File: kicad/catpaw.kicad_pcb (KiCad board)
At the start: 2 copper layers, 80 x 75 mm, 34 parts, among them J3 m12,Acode,5pin,femalesocket (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, J4 m8, 4Pin Supply Connector FEM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, SW1 1MD1T1B1M6QES, U1 INA826, U2 LM1458mx

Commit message: pcbnew initial route
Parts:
- C1, R1, R2, R3, R8, U1: moved to B.Cu
- C2: renamed from C3; moved to B.Cu
- R10: renamed from R9; moved to B.Cu
- R11: renamed from R10; moved to B.Cu
- R4: renamed from R5; moved to B.Cu
- R5: renamed from R6; moved to B.Cu
- R6: renamed from R7; moved to B.Cu
- R7: renamed from R4; moved to B.Cu
- R9: renamed from R11; moved to B.Cu
- moved R14 86.1 mm to (126.0, 45.5)
- moved R12 84.8 mm to (142.3, 49.5), turned to -90 degrees
- moved R13 82.7 mm to (145.3, 49.5), turned to -90 degrees
- moved R15 78.6 mm to (126.0, 48.0), turned to 180 degrees
- moved R16 78.0 mm to (126.0, 51.6), turned to 180 degrees
- moved C3 77.0 mm to (132.0, 45.2)
- moved U2 75.7 mm to (132.3, 49.0)
- moved C4 72.4 mm to (129.8, 53.7), turned to 90 degrees
- moved R1 67.2 mm to (139.6, 84.6)
- moved R2 67.2 mm to (145.2, 84.6)
- moved R3 67.2 mm to (150.8, 84.6)
- moved C2 66.0 mm to (170.3, 84.8)
- moved R8 64.1 mm to (156.2, 85.9)
- moved R11 59.7 mm to (172.4, 88.1), turned to 90 degrees
- moved R7 59.4 mm to (152.6, 88.9), turned to -90 degrees
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- renumbered C2 to C3, red to J1, blk to J2
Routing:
- net /Vcc+: track 0.00 -> 98.0 mm, vias 0 -> 3
- net /Vcc-: track 0.00 -> 87.1 mm, vias 0 -> 1
- net /rakout+: track 0.00 -> 43.8 mm
- net /rakout-: track 0.00 -> 41.1 mm
- net Net-(D5-A): track 0.00 -> 20.9 mm, vias 0 -> 1
- net Net-(PS1-AC(L)): track 17.2 -> 0.00 mm
- net /In+ Analog Input: track 0.00 -> 16.9 mm
- net Net-(F1-Pad1): track 18.3 -> 3.17 mm
- net Net-(PS1-AC(N)): track 14.2 -> 0.00 mm
- net Net-(D5-K): track 0.00 -> 13.5 mm, vias 0 -> 1
- net Net-(U2B-+): track 0.00 -> 11.5 mm
- net Net-(U2A-+): track 0.00 -> 8.37 mm
- net GND: track 0.00 -> 7.24 mm
- added copper zone on B.Cu, net GND
- added copper zone on F.Cu, net GND

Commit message: pcbnew route v02
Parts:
- C3, C4, R12, R13, R14, R15, R16, U2: moved to B.Cu
- moved R15 34.3 mm to (148.8, 73.5), turned to 0 degrees
- moved R16 33.8 mm to (148.2, 77.1), turned to 0 degrees
- moved C4 28.7 mm to (143.6, 78.9), turned to 0 degrees
- moved U2 27.3 mm to (141.9, 74.5), turned to 180 degrees
- moved C3 25.7 mm to (139.4, 69.8), turned to -90 degrees
- moved R12 12.4 mm to (137.4, 61.0), turned to 90 degrees
- moved R13 11.7 mm to (147.6, 61.0), turned to 90 degrees
- moved C1 2.54 mm to (168.5, 94.7)
- moved R14 2.40 mm to (124.0, 46.7)
- moved R11 2.21 mm to (173.2, 90.2)
- moved R10 2.03 mm to (160.3, 90.6)
- moved R8 2.03 mm to (156.2, 87.9)
- moved R9 2.03 mm to (156.2, 93.2)
- moved U1 2.03 mm to (166.6, 90.6)
- moved C2 1.88 mm to (169.7, 86.6)
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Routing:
- net /Vcc+: track 98.0 -> 60.9 mm
- net /Vcc-: track 87.1 -> 50.2 mm, vias 1 -> 2
- net Net-(PS1-AC(L)): track 0.00 -> 27.4 mm
- net Net-(D5-A): track 20.9 -> 43.5 mm
- net /VACin+: track 22.9 -> 44.7 mm
- net Net-(U2B-+): track 11.5 -> 28.2 mm
- net /VACin-: track 42.6 -> 55.6 mm
- net /m8 GNDp: track 0.00 -> 12.8 mm
- net /m8 Up: track 0.00 -> 11.8 mm
- net Net-(PS1-AC(N)): track 0.00 -> 9.51 mm
- net /m8 GNDs: track 0.00 -> 9.06 mm
- net /m8 Us: track 0.00 -> 9.00 mm
- net Net-(U1--): track 0.00 -> 7.24 mm
- net Net-(U1-+): track 0.00 -> 7.24 mm
- net GND: track 7.24 -> 0.00 mm, vias 0 -> 138
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- added copper zone on B.Cu, net /Vcc+
- added copper zone on B.Cu, net /Vcc-
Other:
- board text added: "blk"
- board text added: "red"

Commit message: pcbnew route03
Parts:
- moved C3 3.94 mm to (143.4, 69.8)
- moved C4 3.94 mm to (147.5, 78.9)
- moved R15 3.94 mm to (152.8, 73.5)
- moved R16 3.94 mm to (152.2, 77.1)
- moved U2 3.94 mm to (145.8, 74.5)
- moved R1 1.02 mm to (139.6, 87.4)
- moved R2 1.02 mm to (145.2, 87.4)
- moved R3 1.02 mm to (150.8, 87.4)
- moved R4 1.02 mm to (139.7, 96.0)
- moved R5 1.02 mm to (145.3, 96.0)
- moved R6 1.02 mm to (150.8, 96.0)
- moved R7 1.02 mm to (152.4, 91.7)
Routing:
- net Net-(D5-A): track 43.5 -> 51.9 mm
- net /Vcc+: track 60.9 -> 56.9 mm
- net /Vcc-: track 50.2 -> 46.3 mm
- net /VACin+: track 44.7 -> 47.4 mm
- net /VACin-: track 55.6 -> 56.8 mm
- net GND: vias 138 -> 121
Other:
- board text added: "M12"
- board text added: "M8"
- board text added: "catpaw rev01 jul26 //keyudits"

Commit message: Exported BOM01, notes to scheme, touched up pcbnew
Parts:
- removed D3, D4: 1N5819, Diode_THT:D_DO-41_SOD81_P10.16mm_Horizontal
- D5: footprint Diode_THT:D_5W_P5.08mm_Vertical_AnodeUp -> LED_THT:LED_D5.0mm_Horizontal_O1.27mm_Z3.0mm
- moved R14 7.39 mm to (116.6, 47.5)
- moved D5 2.75 mm to (111.8, 47.5), turned to -90 degrees
- moved D1 0.25 mm to (172.7, 58.4)
- moved D2 0.25 mm to (169.0, 58.4)
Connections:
- J4 pad 3: /m8 GNDs -> /m8 GNDp
- PS1 pad 4: /rakout- -> /m8 GNDp
- R13 pad 2: /rakout- -> /m8 GNDp
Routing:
- net /rakout-: track 44.3 -> 0.00 mm
- net /m8 GNDp: track 12.8 -> 39.0 mm
- net /m8 GNDs: track 9.06 -> 0.00 mm
- net Net-(D5-K): track 10.9 -> 4.10 mm
- net Net-(D5-A): track 51.9 -> 58.7 mm
- net /Vcc+: track 56.9 -> 59.2 mm, vias 3 -> 8
- net /In+ Analog Input: track 15.4 -> 14.5 mm
- net /Vcc-: track 46.3 -> 47.2 mm, vias 2 -> 5
- net GND: vias 121 -> 127

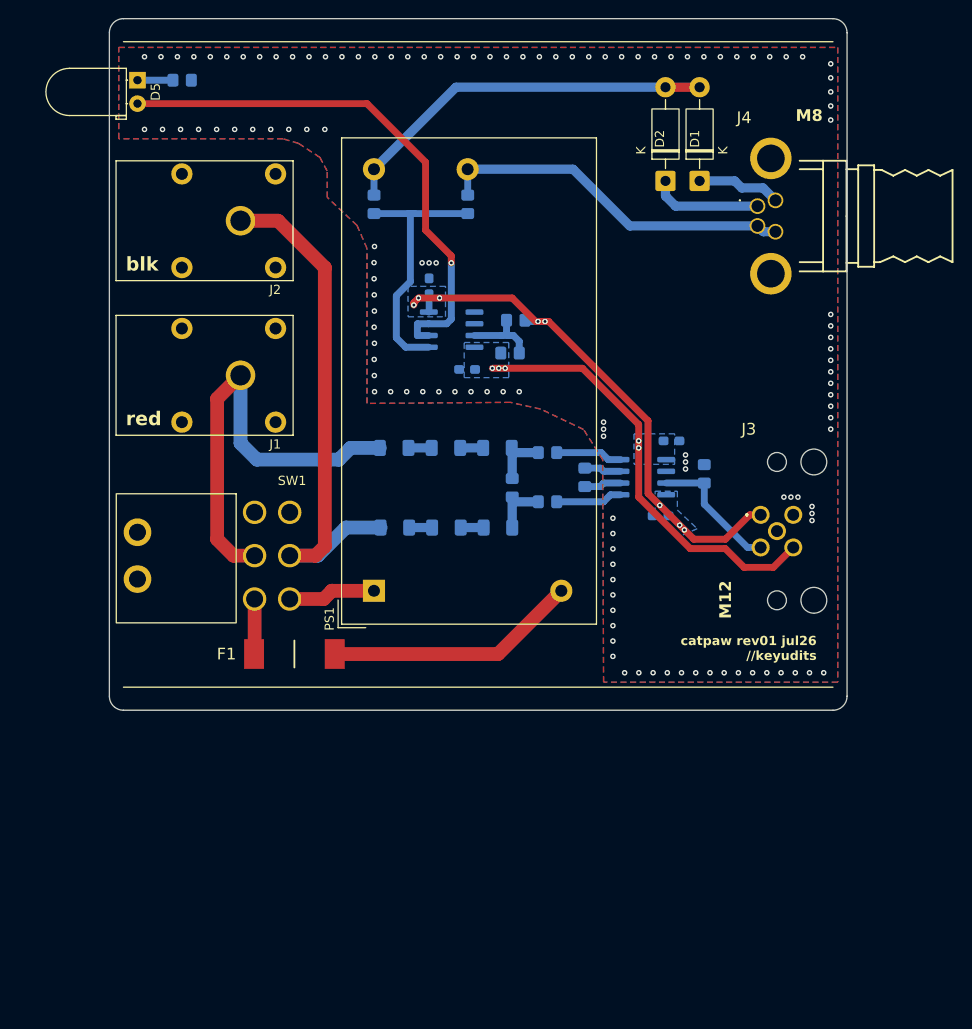
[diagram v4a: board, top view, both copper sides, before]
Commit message: adjusted i/o placement
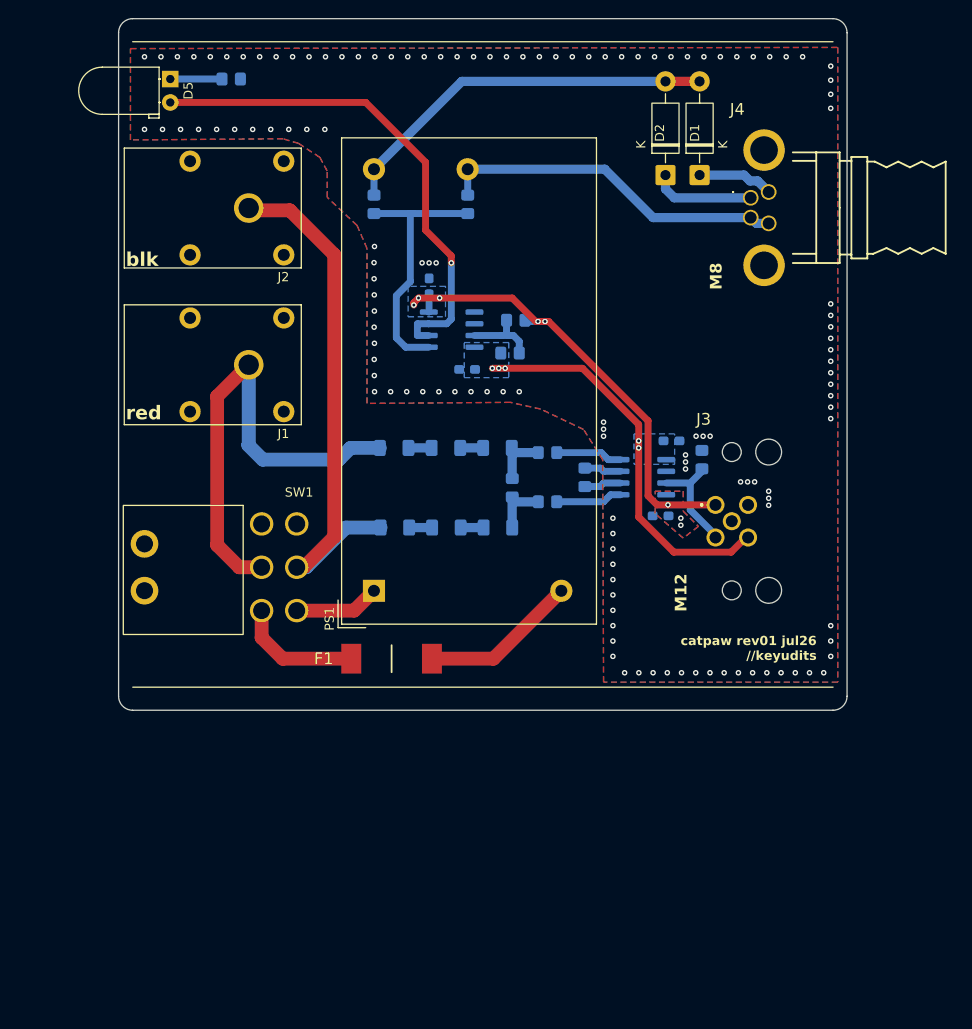
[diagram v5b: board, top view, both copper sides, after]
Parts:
- moved F1 10.6 mm to (139.3, 110.2)
- moved R14 5.32 mm to (121.9, 47.4)
- moved J3 5.02 mm to (174.4, 93.6)
- moved D5 3.56 mm to (115.3, 47.4)
- moved J2 1.64 mm to (123.8, 61.4)
- moved R11 1.56 mm to (173.0, 88.6)
- moved SW1 1.47 mm to (125.2, 100.4)
- moved J1 1.45 mm to (123.8, 78.4)
- moved J4 1.17 mm to (180.2, 59.6)
- moved D1 0.64 mm to (172.7, 57.8)
- moved D2 0.64 mm to (169.0, 57.8)
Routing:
- net Net-(PS1-AC(L)): track 27.4 -> 17.1 mm
- net Net-(F1-Pad1): track 6.03 -> 13.6 mm
- net /Vcc+: track 59.2 -> 51.8 mm
- net /Vcc-: track 47.2 -> 42.7 mm
- net Net-(D5-A): track 58.7 -> 54.9 mm
- net /VACin+: track 47.4 -> 51.0 mm
- net /In+ Analog Input: track 14.5 -> 11.5 mm
- net Net-(D5-K): track 4.10 -> 5.60 mm
- net /VACin-: track 56.8 -> 58.2 mm
- net /m8 GNDp: track 39.0 -> 37.9 mm
- net /m8 Us: track 9.11 -> 8.25 mm
- net /m8 Up: track 11.8 -> 11.1 mm
- net GND: vias 127 -> 132
- added copper zone on F.Cu, net /Vcc+
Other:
- board size 80 x 75 mm -> 79 x 75 mm
- board text added: "dimensions: 75mm wide (hammond callout) 79mm long (1mm less than hammond case)"

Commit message: added test points and jumpers
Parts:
- added GND: Conn_01x01_Pin, Connector_PinHeader_2.54mm:PinHeader_1x01_P2.54mm_Vertical, F.Cu at (182.4, 76.8)
- added R18: 0, Resistor_THT:R_Axial_DIN0204_L3.6mm_D1.6mm_P2.54mm_Vertical, F.Cu at (171.1, 75.6)
- added R19: 0, Resistor_THT:R_Axial_DIN0204_L3.6mm_D1.6mm_P2.54mm_Vertical, F.Cu at (175.3, 75.6)
- added VCC: 0, Resistor_SMD:R_0805_2012Metric_Pad1.20x1.40mm_HandSolder, F.Cu at (168.1, 76.6)
- added VEE: 0, Resistor_SMD:R_0805_2012Metric_Pad1.20x1.40mm_HandSolder, F.Cu at (178.2, 76.6)
- moved R1 0.66 mm to (138.9, 87.4)
- moved R4 0.66 mm to (139.0, 96.0)
- moved R2 0.34 mm to (144.9, 87.4)
- moved R5 0.33 mm to (144.9, 96.0)
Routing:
- net /m8 Up: track 11.1 -> 32.7 mm
- net /m8 GNDp: track 37.9 -> 55.2 mm
- net /Vcc-: track 42.7 -> 55.9 mm, vias 5 -> 6
- net /Vcc+: track 51.8 -> 60.6 mm
- net /VACin-: track 58.2 -> 57.5 mm
- net /VACin+: track 51.0 -> 50.3 mm
- net GND: vias 132 -> 135
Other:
- board text added: "JLCJLCJLCJLCJLC"

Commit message: updated gerbers, rev01 ordered
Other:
- board text removed: "JLCJLCJLCJLCJLC"
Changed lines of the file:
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@@
-		)
-	)
-	(gr_text "JLCJLCJLCJLCJLC"
-		(at 180.721 110.744 -0)
-		(layer "B.SilkS")
-		(effects
-			(font
-				(size 1 1)
-				(thickness 0.1)
-			)
-			(justify left bottom mirror)
 		)
 	)

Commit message: updated parts.numbers, added bode plots
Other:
- board text added: "adjust vcc/vee jumper footprint to 2.54 vertical header pins"
- board text added: "amphenol gives 5.8mm to pcb edge see m12 tech datasheet"
- board text added: "move f1 away from exposed vac pad (8mm)"
- board text added: "rac15-24sk/480"
- board text added: "rac20-24sk/277"
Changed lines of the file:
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@@
+		(layer "User.2")
+	)
+	(gr_rect
+		(start 210.886 53.34)
+		(end 250.886 106.34)
+		(stroke
+			(width 0.1)
+			(type solid)
+		)
+		(fill no)
 		(layer "User.2")
 	)
@@
 		)
 	)
+	(gr_text "adjust vcc/vee jumper footprint to 2.54 vertical header pins"
+		(at 170.434 36.449 0)
+		(layer "User.2")
+		(effects
+			(font
+				(size 1 1)
+				(thickness 0.25)
+				(bold yes)
+			)
+			(justify left bottom)
+		)
+	)
+	(gr_text "amphenol gives 5.8mm to pcb edge\nsee m12 tech datasheet"
+		(at 191.008 113.03 0)
+		(layer "User.2")
+		(effects
+			(font
+				(size 1 1)
+				(thickness 0.25)
+				(bold yes)
+			)
+			(justify left bottom)
+		)
+	)
+	(gr_text "rac20-24sk/277"
+		(at 160.274 70.993 90)
+		(layer "User.2")
+		(effects
+			(font
+				(size 1 1)
+				(thickness 0.1)
+			)
+			(justify left bottom)
+		)
+	)
 	(gr_text "07/20/26"
 		(at 207.01 193.802 0)
@@
 		)
 	)
+	(gr_text "move f1 away from exposed vac pad (8mm)"
+		(at 130.302 117.983 0)
+		(layer "User.2")
+		(effects
+			(font
+				(size 1 1)
+				(thickness 0.25)
+				(bold yes)
+			)
+			(justify left bottom)
+		)
+	)
 	(gr_text "dimensions:	75mm wide (hammond callout)\n			79mm long (1mm less than hammond case)"
 		(at 233.934 22.352 0)
@@
 			)
 			(justify left bottom)
+		)
+	)
+	(gr_text "rac15-24sk/480"
+		(at 219.71 57.15 0)
+		(layer "User.2")
+		(effects
+			(font
+				(size 1 1)
+				(thickness 0.1)
+			)
+			(justify left bottom)
